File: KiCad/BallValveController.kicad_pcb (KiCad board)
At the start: 2 copper layers, 55.6 x 43.2 mm, 62 parts, among them J1 Screw_Terminal_01x03, J2 Screw_Terminal_01x04, J3 Screw_Terminal_01x04, J4 Screw_Terminal_01x04, J5 Conn_01x01_Male, J6 Screw_Terminal_01x04, J7 Screw_Terminal_01x02, K1 G5V-2, Q1 Q_PMOS_GDS, Q2 2N2222A, U2 L7805, U3 XIAO-ESP32-C6, U4 TPS561201/08 or TPS563200

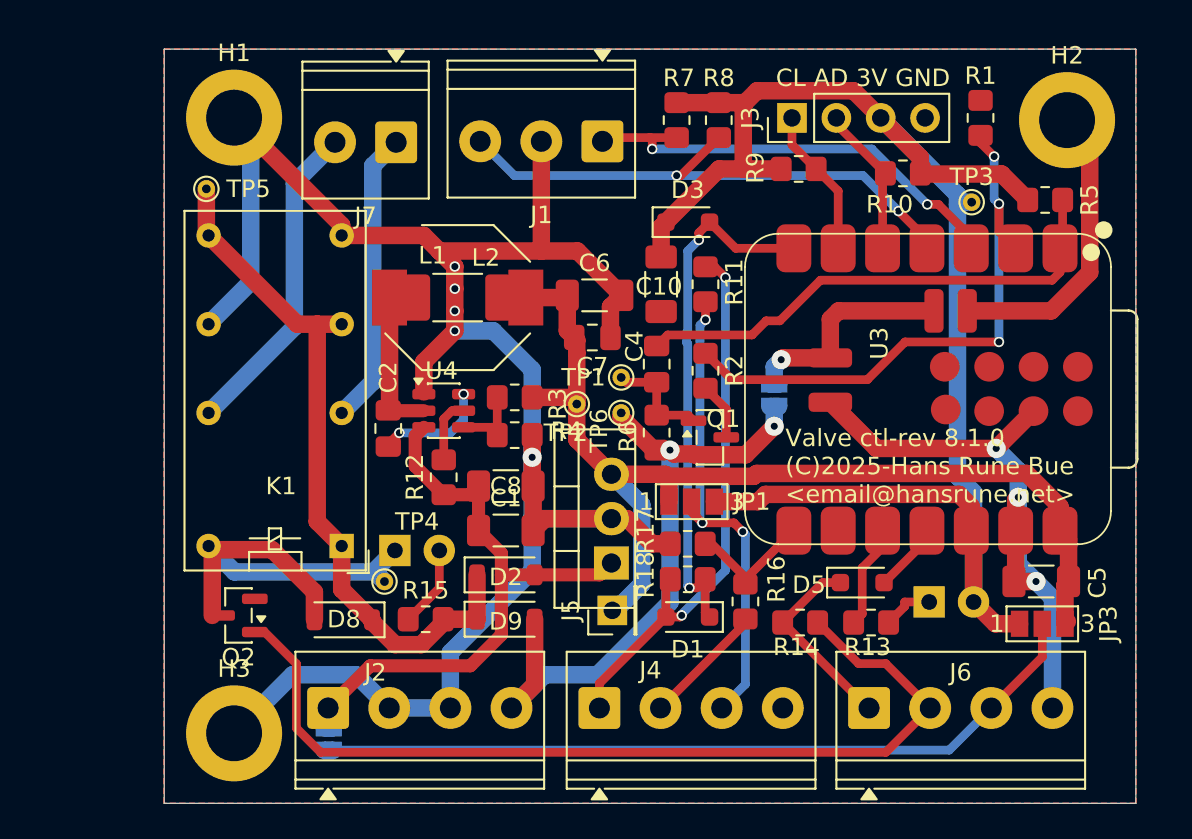
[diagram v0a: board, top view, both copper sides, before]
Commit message: Small layout change for buck feedback loop
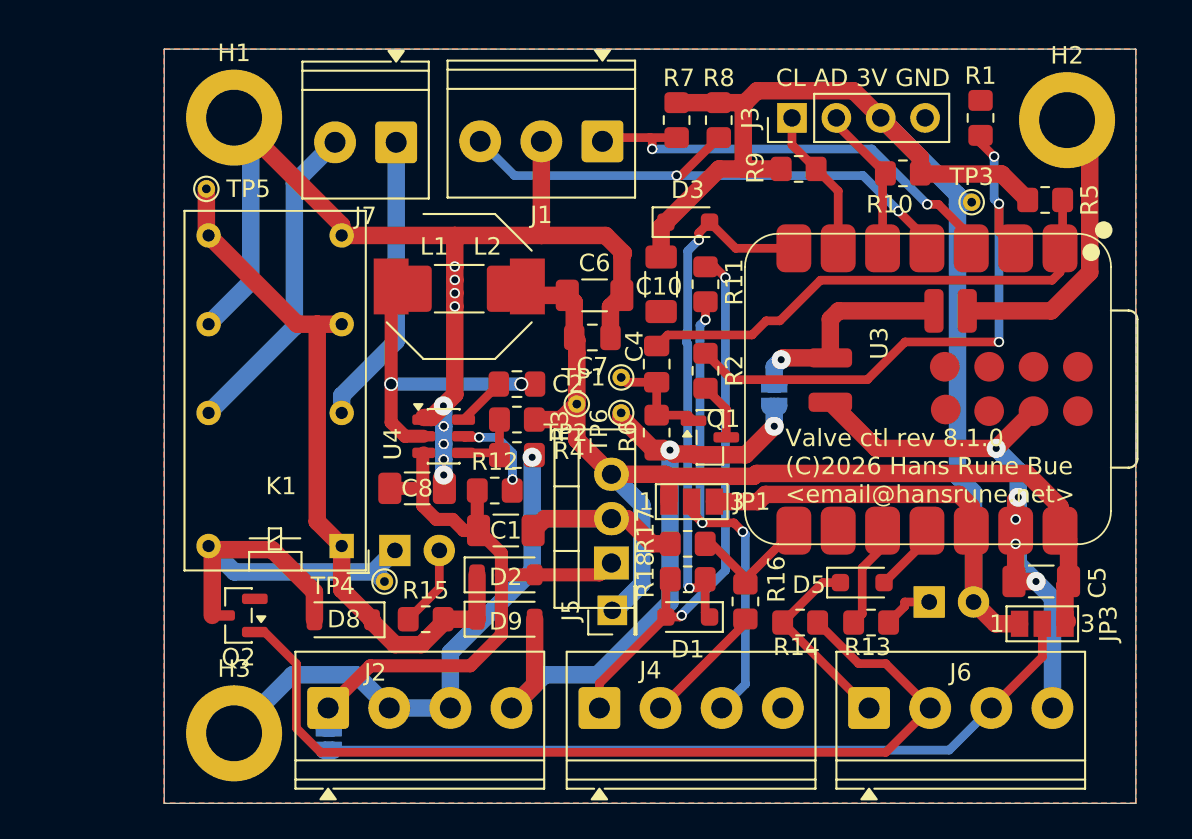
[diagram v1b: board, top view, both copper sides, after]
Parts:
- moved C2 7.79 mm to (156.1, 100.3), turned to 0 degrees
- moved C8 5.08 mm to (150.4, 106.3)
- moved R12 3.02 mm to (154.8, 106.4), turned to 0 degrees
- moved U4 1.46 mm to (151.9, 103.3)
- moved R3 1.28 mm to (156.1, 102.4)
- moved R4 1.15 mm to (156.1, 104.4)
- moved L2 0.64 mm to (152.8, 94.7)
- moved L1 0.52 mm to (152.8, 94.9)
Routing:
- net /IND1: track 8.68 -> 18.2 mm, vias 0 -> 2
- net GND: track 171.3 -> 163.1 mm, vias 8 -> 15
- net Net-(U4-VBST): track 6.51 -> 2.87 mm, vias 2 -> 0
- net Net-(U4-EN): track 3.67 -> 5.36 mm, vias 0 -> 2
- net /PwrIn: track 34.2 -> 35.8 mm
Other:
- board text added: "Valve ctl rev 8.1.0 (C)2026 Hans Rune Bue <email@hansrune.net>"
- board text added: "Valve ctl rev 8.1.0 (C)2026-Hans Rune Bue <email@hansrune.net>"
- board text removed: "Valve ctl-rev 8.1.0 (C)2025-Hans Rune Bue <email@hansrune.net>"

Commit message: Rearranged resistors - stricter fill clearances
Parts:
- moved R11 18.3 mm to (168.8, 112.8)
- moved D3 2.85 mm to (166.9, 93.7), turned to -90 degrees
- moved R16 1.78 mm to (170.9, 112.8)
- moved R14 1.45 mm to (173.1, 112.8), turned to -90 degrees
- moved D5 0.55 mm to (176.4, 111.8)
- moved C10 0.47 mm to (164.3, 94.1)
- moved R18 0.38 mm to (165.9, 111.9)
- moved D1 0.28 mm to (165.7, 113.9)
- moved R13 0.25 mm to (176.5, 113.8)
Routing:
- net /TX: track 31.8 -> 14.2 mm, vias 2 -> 0
- net Net-(J4-Pin_3): track 27.6 -> 15.1 mm, vias 3 -> 2
- net GND: track 163.1 -> 175.6 mm, vias 15 -> 17
- net Net-(D1-K): track 30.4 -> 26.2 mm
- net +3V3: track 91.9 -> 94.0 mm
- net /RX: track 7.11 -> 8.75 mm
- net /IHigh: track 11.2 -> 10.1 mm
- net /ILow: track 52.6 -> 51.9 mm

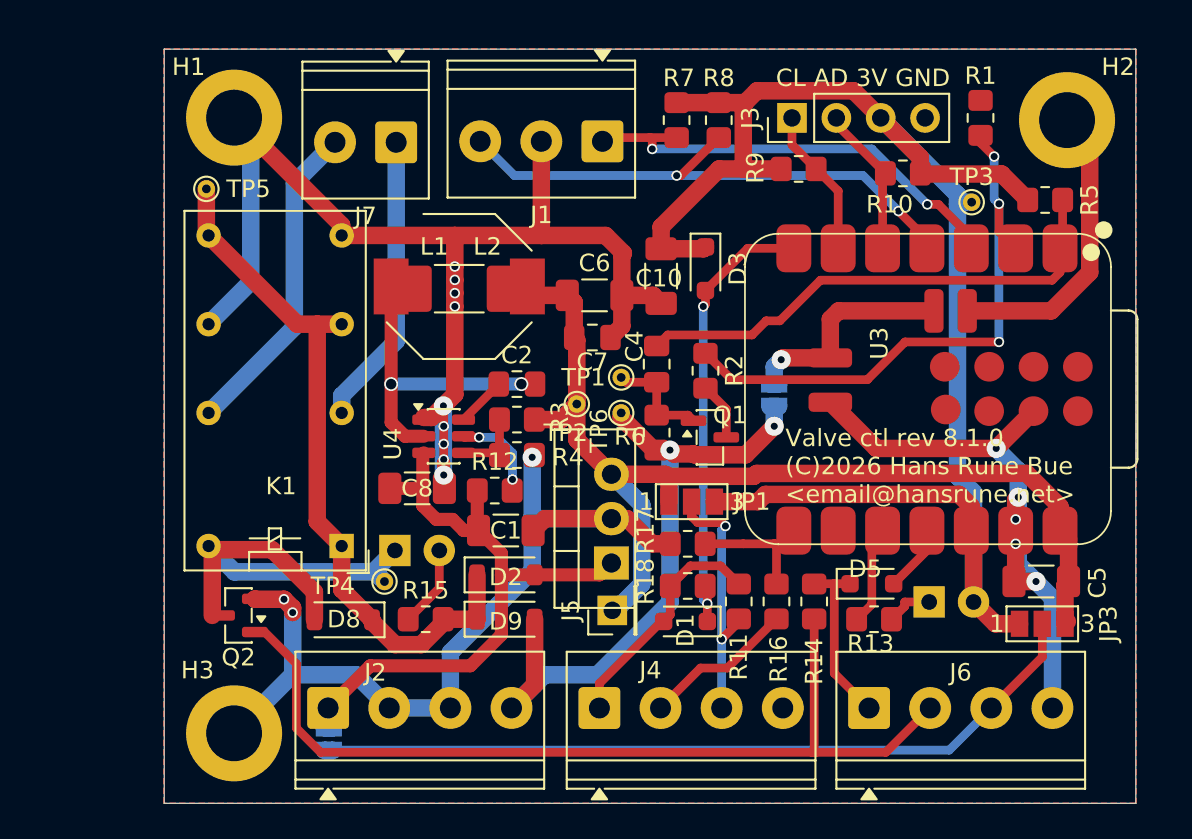
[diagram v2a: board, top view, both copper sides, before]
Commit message: GND zones update
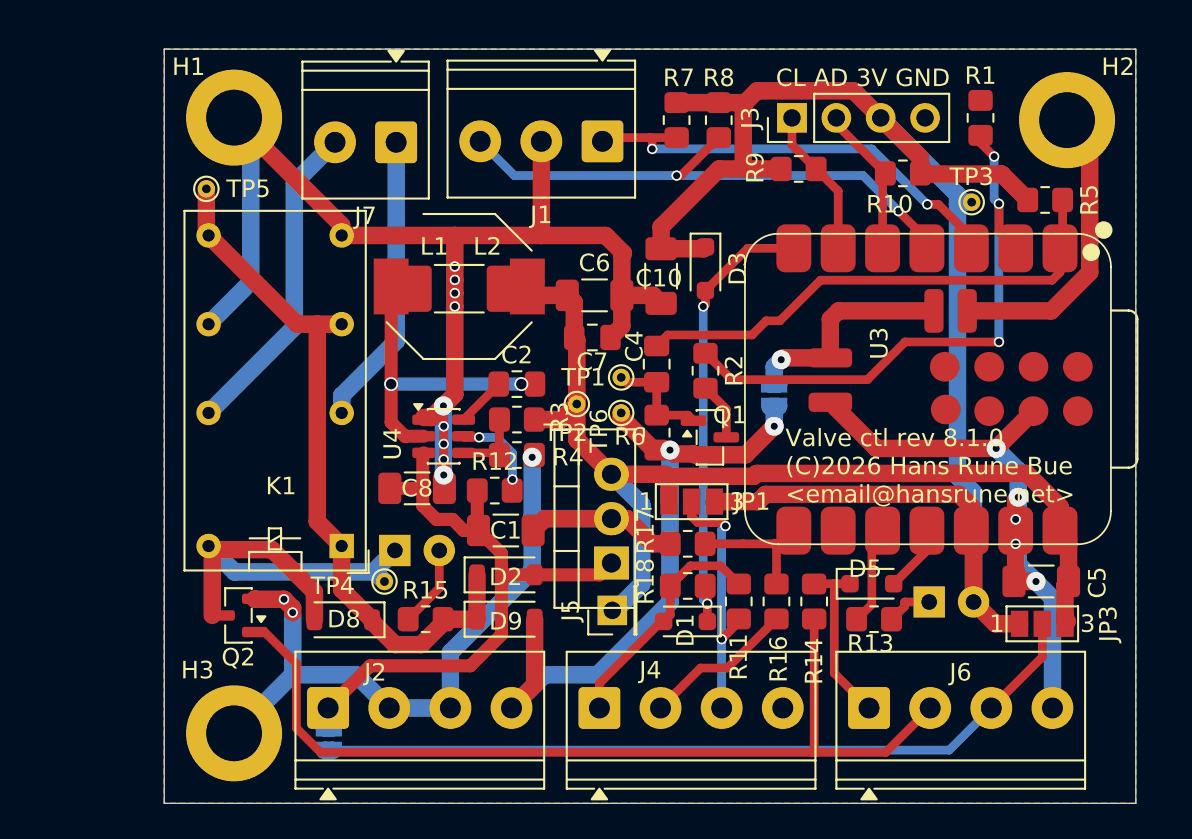
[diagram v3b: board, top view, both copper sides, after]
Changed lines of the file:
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@@
 		(net 1)
 		(net_name "GND")
-		(layers "F.Cu" "B.Cu")
+		(layer "B.Cu")
+		(name "BZoneGND")
 		(hatch edge 0.508)
 		(connect_pads

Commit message: ME3116 layout
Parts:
- removed U4: TPS561201/08 or TPS563200, Package_TO_SOT_SMD:SOT-23-6
- added 1: ~, Package_TO_SOT_SMD:SOT-23-6, F.Cu at (152.0, 103.0)
- added C3: 470nF, Capacitor_SMD:C_0805_2012Metric_Pad1.18x1.45mm_HandSolder, F.Cu at (156.1, 102.5)
- added D4: SS34, Diode_SMD:D_SMA, F.Cu at (161.7, 92.1)
- moved R12 6.82 mm to (148.8, 103.1), turned to 90 degrees
- moved C2 6.35 mm to (149.7, 100.2), turned to 180 degrees
- moved C10 3.20 mm to (166.9, 92.2), turned to 90 degrees
- moved D3 2.29 mm to (166.8, 96.0), turned to 0 degrees
- moved R3 1.91 mm to (156.1, 100.5)
- moved R4 0.25 mm to (156.1, 104.6)
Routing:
- net +5V: track 61.2 -> 94.6 mm, vias 0 -> 5
- net /IND1: track 18.2 -> 5.54 mm, vias 2 -> 0
- net GND: track 175.6 -> 183.1 mm, vias 17 -> 12
- net +3V3: track 94.0 -> 86.9 mm
- net Net-(1-BS): track 2.87 -> 7.23 mm, vias 0 -> 2
- net Net-(1-EN): track 5.36 -> 2.07 mm, vias 2 -> 0
- net Net-(1-FB): track 4.14 -> 6.76 mm
- net Net-(D1-K): track 26.2 -> 24.6 mm

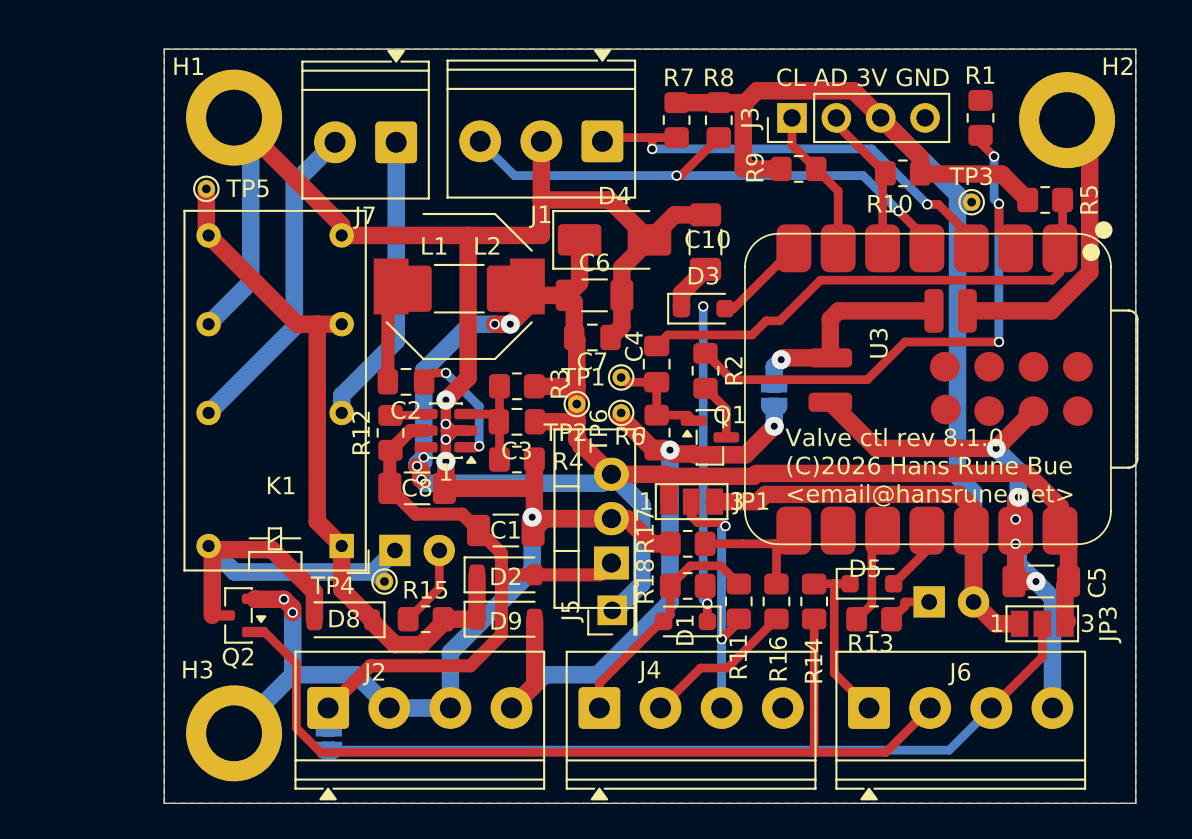
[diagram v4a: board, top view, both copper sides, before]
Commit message: ME3116 dual layout
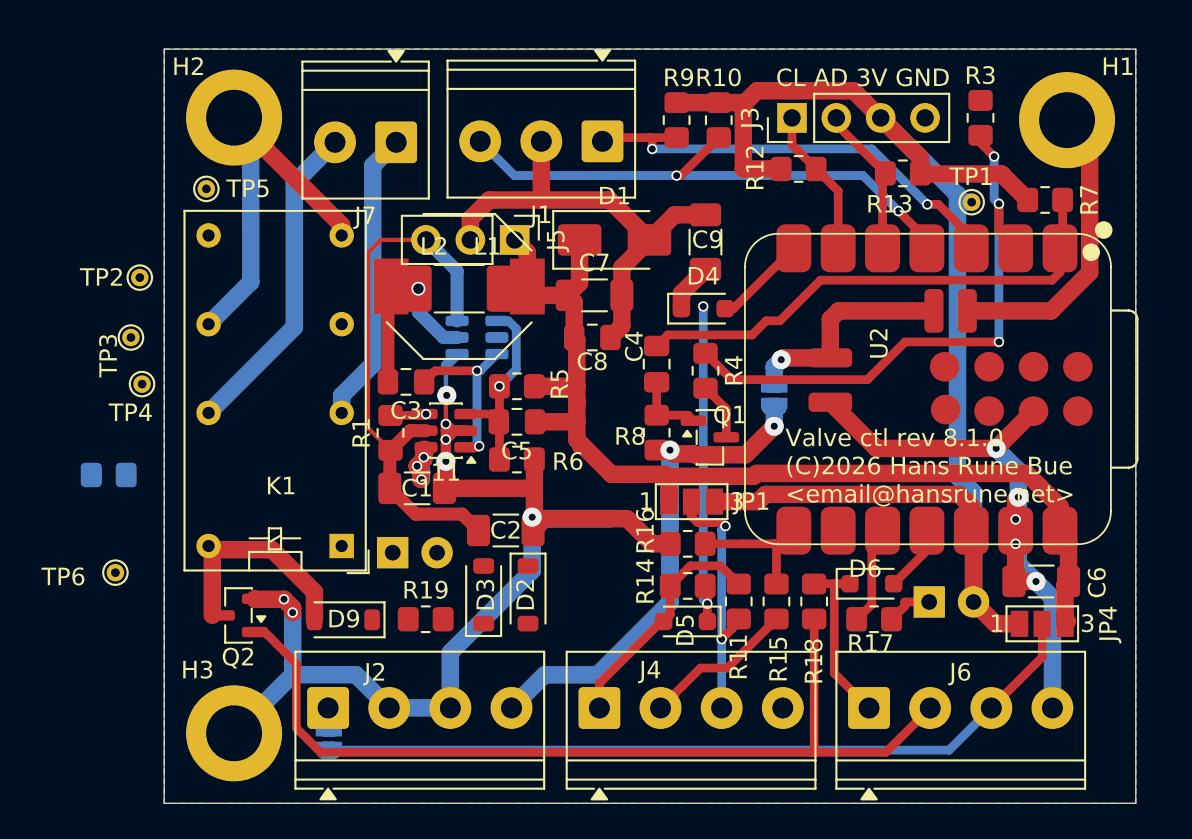
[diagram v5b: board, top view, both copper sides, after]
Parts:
- removed the U2 at (161.5, 110.6)
- added R2: 4.7k, Resistor_SMD:R_0805_2012Metric_Pad1.20x1.40mm_HandSolder, B.Cu at (132.7, 105.5)
- added U1: TPS561201/08 or TPS562203 or TPS563203, Package_TO_SOT_SMD:SOT-23-6, B.Cu at (153.8, 97.7)
- J5: value Conn_01x01_Male -> Screw_Terminal_01x03; footprint Connector_PinHeader_2.54mm:PinHeader_1x01_P2.54mm_Vertical -> Connector_PinHeader_2.54mm:PinHeader_1x03_P2.54mm_Vertical
- moved TP3 28.4 mm to (134.0, 97.7)
- moved TP2 28.1 mm to (134.5, 94.2)
- moved TP4 24.9 mm to (134.6, 100.3)
- moved J5 21.9 mm to (156.0, 92.1), turned to -90 degrees
- moved TP6 15.4 mm to (133.1, 111.1)
- moved D2 1.89 mm to (156.7, 112.4), turned to -90 degrees
- moved D3 1.71 mm to (154.2, 112.4), turned to 90 degrees
- moved D8 0.18 mm to (149.0, 110.0)
- renumbered 1 to 11, C8 to C1, C1 to C2, C2 to C3, C3 to C5, C5 to C6, C6 to C7, C7 to C8, C10 to C9, D4 to D1, D9 to D2, D2 to D3, D3 to D4, D1 to D5, D5 to D6, D6 to D7, D7 to D8, D8 to D9, H2 to H1, H1 to H2, JP5 to JP2, JP2 to JP3, JP3 to JP4, L2 to L1, L1 to L2, R12 to R1, R8 to R10, R9 to R12, R10 to R13, R18 to R14, R16 to R15, R17 to R16, R13 to R17, R14 to R18, R15 to R19, R1 to R3, R2 to R4, R3 to R5, R4 to R6, R5 to R7, R6 to R8, R7 to R9, TP3 to TP1, TP1 to TP2, TP6 to TP3, TP2 to TP4, TP4 to TP6, U3 to U2
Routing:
- net +VSW: track 40.6 -> 0.00 mm
- net +5V: track 94.6 -> 63.8 mm, vias 5 -> 3
- net GND: track 183.1 -> 168.3 mm
- net /RELAYSW: track 25.1 -> 12.5 mm
- net /VBAT: track 37.6 -> 28.9 mm
- net Net-(11-FB): track 6.76 -> 11.8 mm, vias 0 -> 1
- net Net-(D8-A): track 4.67 -> 0.00 mm
- net /IND1: track 5.54 -> 9.70 mm, vias 0 -> 1
- net /PwrIn: track 35.5 -> 31.6 mm
- net Net-(11-BS): track 7.23 -> 9.99 mm
- net Net-(Q1-G): track 6.27 -> 4.13 mm
- net Net-(11-EN): vias 0 -> 1
